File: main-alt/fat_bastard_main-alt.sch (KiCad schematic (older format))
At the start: 57 parts, among them J1 INPUT, J2 TO_LD_12V, J3 TO_LD_IN, J4 TO_LD_GAIN, J5 TO_LD_OUT, J6 12V_IN, J8 FOOTSW, J9 OUTPUT, K1 FINDER-30.22, U1 OPA2134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

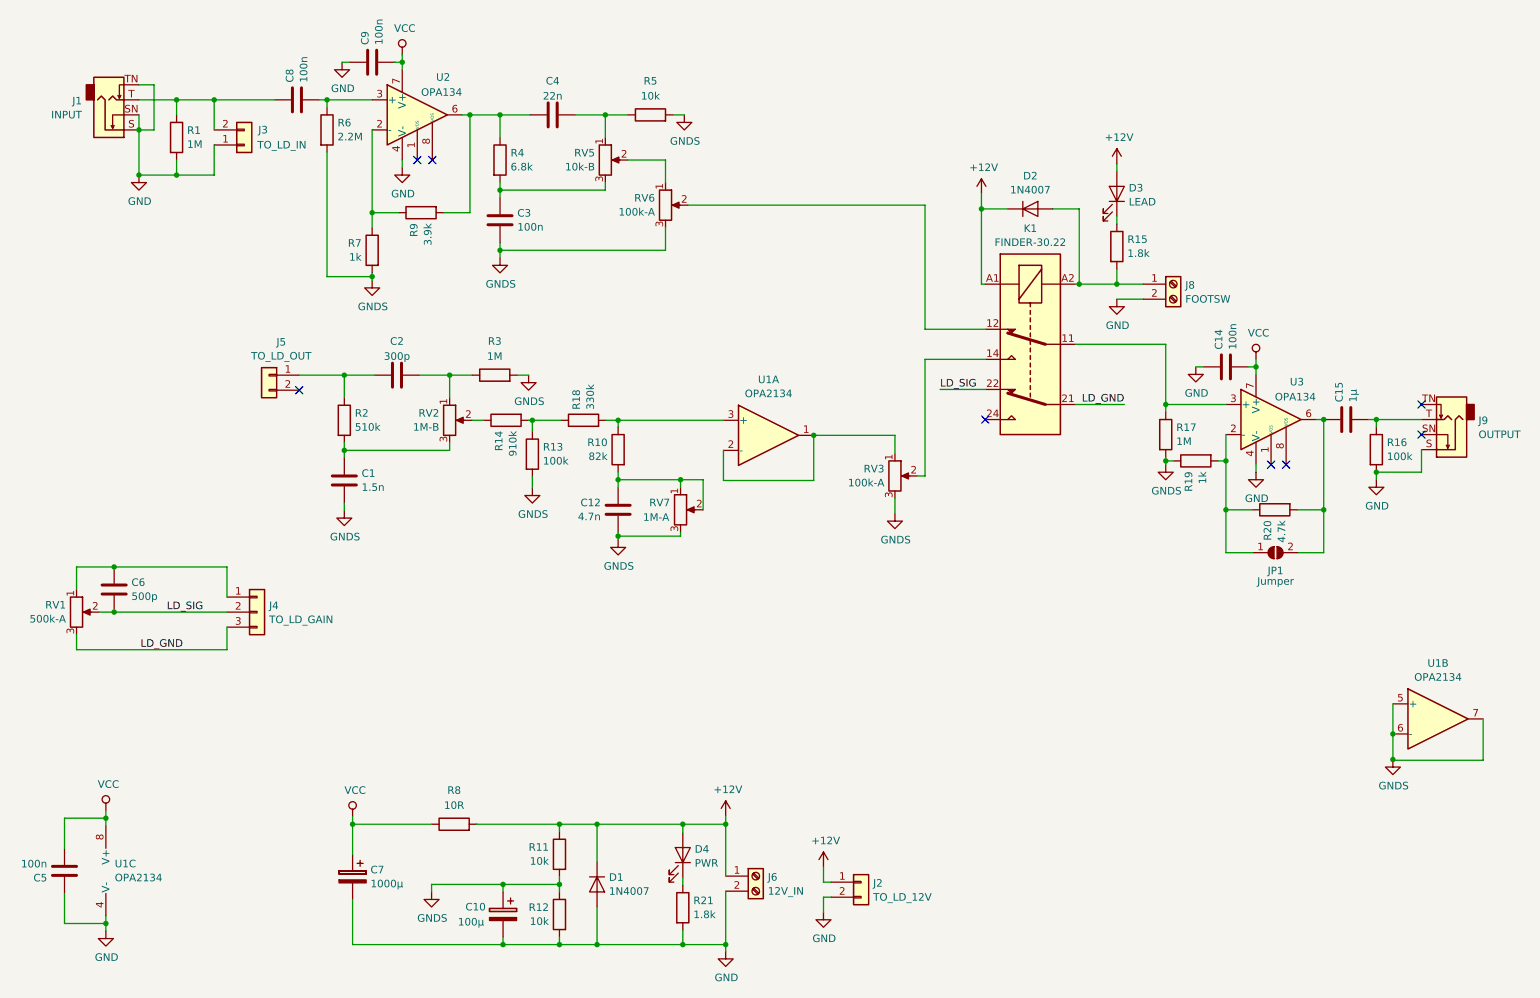
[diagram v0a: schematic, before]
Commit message: Fix potentiometers orientation
Signed-off-by: Arnaud Ferraris <arnaud.ferraris@gmail.com>
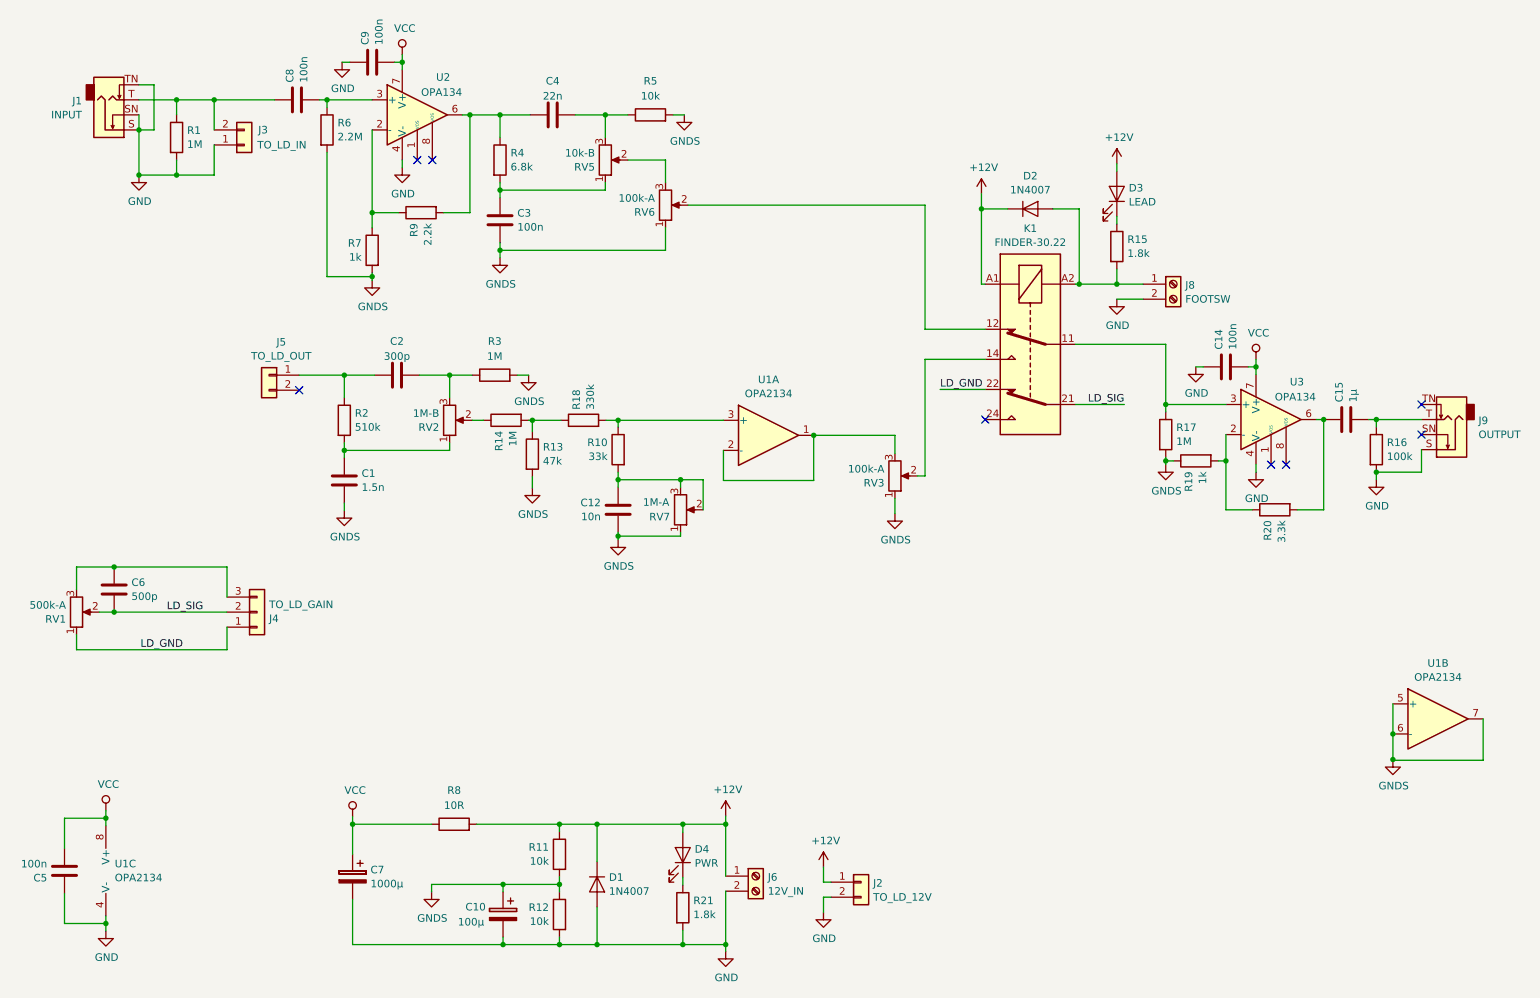
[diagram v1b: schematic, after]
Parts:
- removed JP1: Jumper, Jumper:SolderJumper-2_P1.3mm_Open_TrianglePad1.0x1.5mm, symbol Jumper:SolderJumper_2_Open
- C12: value 4.7n -> 10n
- R10: value 82k -> 33k
- R13: value 100k -> 47k
- R14: value 910k -> 1M
- R20: value 4.7k -> 3.3k
- R9: value 3.9k -> 2.2k
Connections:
- net GNDS: now also RV3.1, RV6.1, RV7.1; no longer RV3.3, RV6.3, RV7.3
- net LD_GND: now also J4.1 (Pin_1), K1.22, RV1.1; no longer J4.3 (Pin_3), K1.21, RV1.3
- net LD_SIG: now also K1.21; no longer K1.22
- net at C4.2, R5.1: now also RV5.3; no longer RV5.1
- net at RV5.2: now also RV6.3; no longer RV6.1
- net at C3.2, R4.2: now also RV5.1; no longer RV5.3
- net at C12.2, R10.2, RV7.2: now also RV7.3; no longer RV7.1
- net at C2.2, R3.1: now also RV2.3; no longer RV2.1
- net at C1.2, R2.2: now also RV2.1; no longer RV2.3
- net at U1.1, U1.2 (-): now also RV3.3; no longer RV3.1
- new net: C6.2, J4.3 (Pin_3), RV1.3
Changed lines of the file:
@@
 F 3 "~" H 2310 5005 50  0001 C CNN
 	1    2310 5005
-	1    0    0    -1
+	1    0    0    1
 $EndComp
 $Comp
@@
 F 3 "~" H 1110 5005 50  0001 C CNN
 	1    1110 5005
-	1    0    0    -1
+	1    0    0    1
 $EndComp
 $Comp
@@
 F 3 "~" H 3590 3730 50  0001 C CNN
 	1    3590 3730
-	1    0    0    -1
+	1    0    0    1
 $EndComp
 $Comp
@@
 F 3 "~" H 6550 4100 50  0001 C CNN
 	1    6550 4100
-	1    0    0    -1
+	1    0    0    1
 $EndComp
 $Comp
@@
 F 3 "~" H 4625 2000 50  0001 C CNN
 	1    4625 2000
-	1    0    0    -1
+	1    0    0    1
 $EndComp
 $Comp
@@
 F 3 "~" H 5025 2300 50  0001 C CNN
 	1    5025 2300
-	1    0    0    -1
+	1    0    0    1
 $EndComp
 $Comp
@@
 F 3 "~" H 5125 4325 50  0001 C CNN
 	1    5125 4325
-	1    0    0    -1
+	1    0    0    1
 $EndComp
 $Comp
@@
 	8750 3825 8750 4000
 Connection ~ 9400 3725
+Text Label 8075 3625 2    50   ~ 0
+LD_SIG
 Text Label 6850 3525 0    50   ~ 0
-LD_SIG
-Text Label 8075 3625 2    50   ~ 0
 LD_GND
 Wire Wire Line
@@
 AR Path="/5C728193/5C74E1E0" Ref="R?"  Part="1"
 F 0 "R10" H 4780 3972 50  0000 L CNN
-F 1 "82k" H 4780 3879 50  0000 L CNN
+F 1 "33k" H 4780 3879 50  0000 L CNN
 F 2 "Resistor_THT:R_Axial_DIN0309_L9.0mm_D3.2mm_P12.70mm_Horizontal" V 4640 3925 50  0001 C CNN
 F 3 "~" H 4710 3925 50  0001 C CNN
@@
 AR Path="/5C728193/5C74E3E2" Ref="C?"  Part="1"
 F 0 "C12" H 4595 4278 50  0000 R CNN
-F 1 "4.7n" H 4595 4371 50  0000 R CNN
+F 1 "10n" H 4595 4371 50  0000 R CNN
 F 2 "Capacitor_THT:C_Rect_L7.2mm_W3.0mm_P5.00mm_FKS2_FKP2_MKS2_MKP2" H 4748 4175 50  0001 C CNN
 F 3 "~" H 4710 4325 50  0001 C CNN
@@
 AR Path="/5C728193/5C74EF3D" Ref="R?"  Part="1"
 F 0 "R9" H 3470 2397 50  0000 L CNN
-F 1 "3.9k" H 3470 2304 50  0000 L CNN
+F 1 "2.2k" H 3470 2304 50  0000 L CNN
 F 2 "Resistor_THT:R_Axial_DIN0309_L9.0mm_D3.2mm_P12.70mm_Horizontal" V 3330 2350 50  0001 C CNN
 F 3 "~" H 3400 2350 50  0001 C CNN
@@
 AR Path="/5C728193/5C7DA71C" Ref="R?"  Part="1"
 F 0 "R14" H 4035 3777 50  0000 L CNN
-F 1 "910k" H 4035 3684 50  0000 L CNN
+F 1 "1M" H 4035 3684 50  0000 L CNN
 F 2 "Resistor_THT:R_Axial_DIN0309_L9.0mm_D3.2mm_P12.70mm_Horizontal" V 3895 3730 50  0001 C CNN
 F 3 "~" H 3965 3730 50  0001 C CNN
@@
 AR Path="/5C728193/5C7221A2" Ref="R?"  Part="1"
 F 0 "R13" H 4210 4002 50  0000 L CNN
-F 1 "100k" H 4210 3909 50  0000 L CNN
+F 1 "47k" H 4210 3909 50  0000 L CNN
 F 2 "Resistor_THT:R_Axial_DIN0309_L9.0mm_D3.2mm_P12.70mm_Horizontal" V 4070 3955 50  0001 C CNN
 F 3 "~" H 4140 3955 50  0001 C CNN
@@
 AR Path="/5C728193/5C779001" Ref="R?"  Part="1"
 F 0 "R20" H 9145 4372 50  0000 L CNN
-F 1 "4.7k" H 9145 4279 50  0000 L CNN
+F 1 "3.3k" H 9145 4279 50  0000 L CNN
 F 2 "Resistor_THT:R_Axial_DIN0309_L9.0mm_D3.2mm_P12.70mm_Horizontal" V 9005 4325 50  0001 C CNN
 F 3 "~" H 9075 4325 50  0001 C CNN
@@
 	4710 3730 5410 3730
 Connection ~ 4710 3730
-$Comp
-L Jumper:SolderJumper_2_Open JP1
-U 1 1 5C97A0C4
-P 9080 4610
-F 0 "JP1" H 9080 4490 50  0000 C CNN
-F 1 "Jumper" H 9080 4420 50  0000 C CNN
-F 2 "Jumper:SolderJumper-2_P1.3mm_Open_TrianglePad1.0x1.5mm" H 9080 4610 50  0001 C CNN
-F 3 "~" H 9080 4610 50  0001 C CNN
-	1    9080 4610
-	1    0    0    -1
-$EndComp
-Wire Wire Line
-	9230 4610 9400 4610
 Wire Wire Line
 	9400 3725 9400 4325
-Connection ~ 9400 4325
-Wire Wire Line
-	9400 4325 9400 4610
-Wire Wire Line
-	8750 4610 8930 4610
 Wire Wire Line
 	8750 4000 8750 4325
-Connection ~ 8750 4325
-Wire Wire Line
-	8750 4325 8750 4610
 Wire Wire Line
 	5410 3930 5410 4130

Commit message: Improve rounting
Signed-off-by: Arnaud Ferraris <arnaud.ferraris@gmail.com>
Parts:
- C2, C6: footprint Capacitor_THT:C_Rect_L10.0mm_W5.0mm_P5.00mm_P7.50mm -> Capacitor_THT:C_Disc_D10.5mm_W5.0mm_P5.00mm
- D4: footprint LED_THT:LED_D3.0mm_Horizontal_O1.27mm_Z2.0mm -> LED_THT:LED_D3.0mm_Horizontal_O3.81mm_Z2.0mm
- R1: value 1M -> 2.2M
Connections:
- net GNDS: no longer U1.5 (+), U1.6 (-), U1.7
- net at R13.1, R14.2: now also U1.3 (+); no longer R18.1
- net at R10.1, R18.2: now also U1.5 (+); no longer U1.3 (+)
- new net: RV3.3, U1.6 (-), U1.7
- new net: R18.1, U1.1, U1.2 (-)
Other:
- moved on the sheet: C1, C12, C2, C6, J4, J5, R10, R13, R14, R18, R2, R3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
